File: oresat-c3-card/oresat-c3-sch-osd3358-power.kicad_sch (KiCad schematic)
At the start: 36 parts, among them Q6 MMBT2907, U1 OSD3358-1G-ISM, U10 SN74AUC1G07DCKR, U14 TLVH431

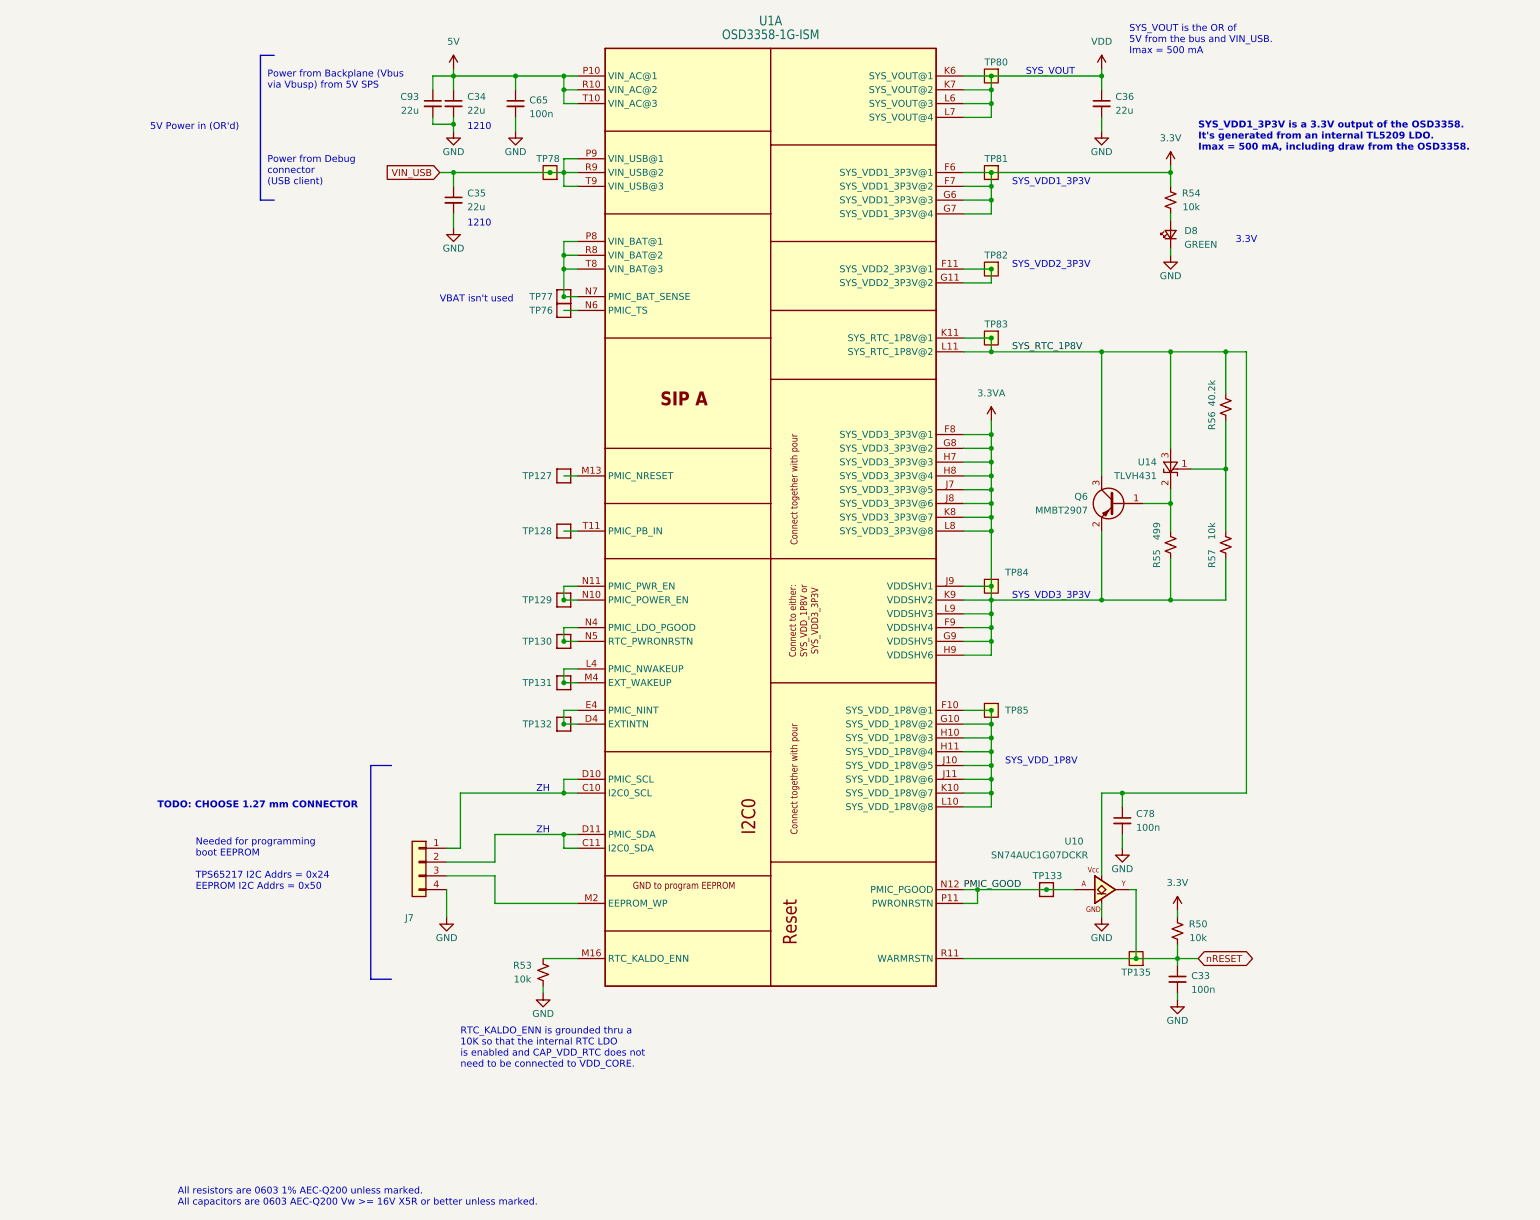
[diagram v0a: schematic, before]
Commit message: All DRC exclusing RF traces are cleaned up.  RF traces cleaned up with mask and bends. Some more notes in the schematic for future us.
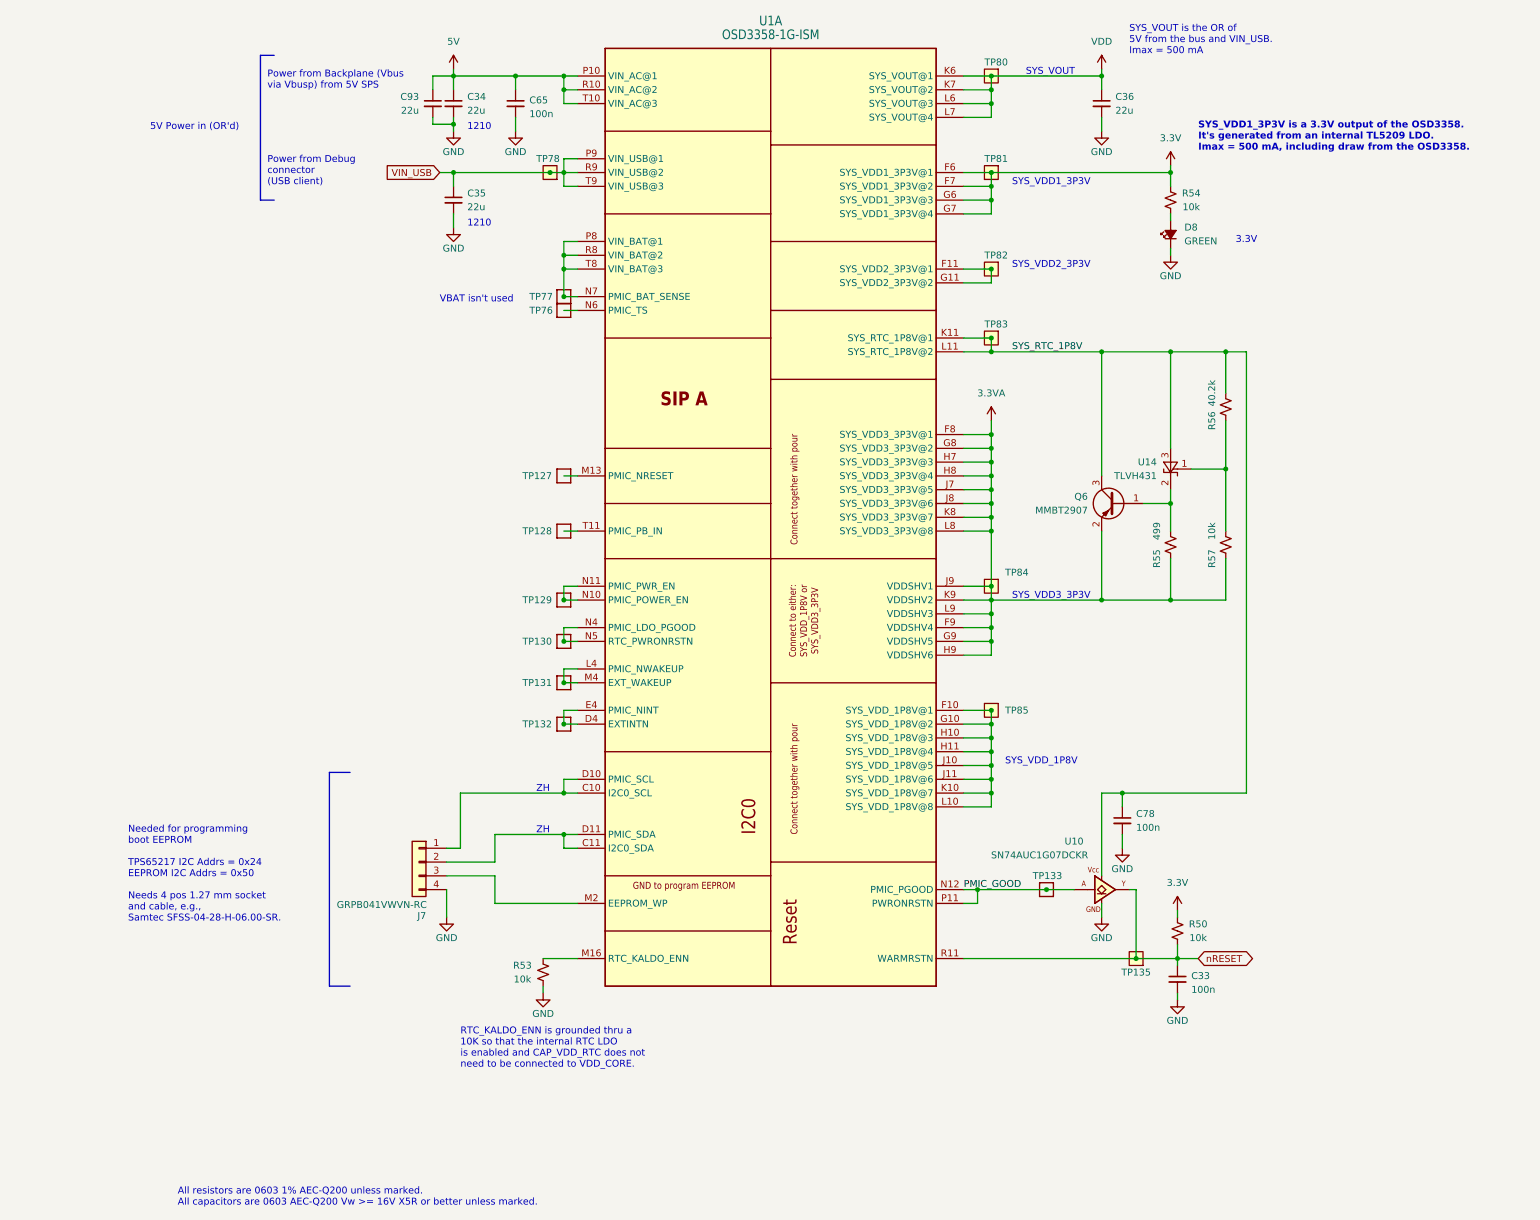
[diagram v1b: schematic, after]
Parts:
- D8: symbol Device:LED_Small -> Device:LED_Small_Filled
- J7: value ~ -> GRPB041VWVN-RC; DPN (none) -> S9014E-04-ND; DST (none) -> DigiKey; MFR (none) -> Sullins Connector Solutions; MPN (none) -> GRPB041VWVN-RC
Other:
- note added: "Needed for programming boot EEPROM TPS65217 I2C Addrs = 0x24 EEPROM I2C Addrs = 0x50 Needs 4 pos 1.27 mm socket and cable, e.g., Samtec SFSS-04-28-H-06.00-SR."
- note removed: "Needed for programming boot EEPROM TPS65217 I2C Addrs = 0x24 EEPROM I2C Addrs = 0x50"
- note removed: "TODO: CHOOSE 1.27 mm CONNECTOR"
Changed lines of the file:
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@@
 		)
 	)
-	(text "TODO: CHOOSE 1.27 mm CONNECTOR"
-		(exclude_from_sim no)
-		(at 130.302 187.706 0)
-		(effects
-			(font
-				(size 1.27 1.27)
-				(thickness 0.254)
-				(bold yes)
-			)
-		)
-	)
 	(text "All resistors are 0603 1% AEC-Q200 unless marked.\nAll capacitors are 0603 AEC-Q200 Vw >= 16V X5R or better unless marked."
 		(exclude_from_sim no)
@@
 		)
 	)
-	(text "Needed for programming\nboot EEPROM\n\nTPS65217 I2C Addrs = 0x24\nEEPROM I2C Addrs = 0x50"
+	(text "Needed for programming\nboot EEPROM\n\nTPS65217 I2C Addrs = 0x24\nEEPROM I2C Addrs = 0x50\n\nNeeds 4 pos 1.27 mm socket\nand cable, e.g., \nSamtec SFSS-04-28-H-06.00-SR."
 		(exclude_from_sim no)
-		(at 118.872 203.454 0)
+		(at 106.426 209.296 0)
 		(effects
 			(font
@@
 	(polyline
 		(pts
-			(xy 151.13 219.71) (xy 154.94 219.71)
+			(xy 143.51 220.98) (xy 147.32 220.98)
 		)
 		(stroke
@@
 	(polyline
 		(pts
-			(xy 154.94 180.34) (xy 151.13 180.34)
+			(xy 147.32 181.61) (xy 143.51 181.61)
 		)
 		(stroke
@@
 	(polyline
 		(pts
-			(xy 151.13 180.34) (xy 151.13 219.71)
+			(xy 143.51 181.61) (xy 143.51 220.98)
 		)
 		(stroke
@@
 	)
 	(symbol
-		(lib_id "Device:LED_Small")
+		(lib_id "Device:LED_Small_Filled")
 		(at 298.45 82.55 90)
 		(unit 1)
@@
 		(fields_autoplaced yes)
 		(property "Reference" "D8"
-			(at 300.99 81.8515 90)
+			(at 300.99 81.2164 90)
 			(effects
 				(font
@@
 		)
 		(property "Value" "GREEN"
-			(at 300.99 84.3915 90)
+			(at 300.99 83.7564 90)
 			(effects
 				(font
@@
 			)
 		)
-		(property "Datasheet" "https://www.we-online.com/components/products/datasheet/150060GS75000.pdf"
+		(property "Datasheet" "~"
 			(at 298.45 82.55 90)
 			(effects
@@
 			)
 		)
-		(property "Description" "Green 520nm LED Indication - Discrete 3.2V 0603 (1608 Metric) - 430 mcd @ 20 mA"
+		(property "Description" "Light emitting diode, small symbol, filled shape"
 			(at 298.45 82.55 0)
 			(effects
@@
 		(dnp no)
 		(property "Reference" "J7"
-			(at 158.242 208.4183 0)
+			(at 160.528 208.026 0)
 			(effects
 				(font
@@
 			)
 		)
-		(property "Value" "~"
-			(at 158.242 205.994 0)
+		(property "Value" "GRPB041VWVN-RC"
+			(at 153.162 205.994 0)
 			(effects
 				(font
@@
 			)
 		)
-		(property "Datasheet" "~"
+		(property "Datasheet" "https://s3.amazonaws.com/catalogspreads-pdf/PAGE94-95%20.050%20MALE%20HDR%20ST%20RA%20SMT.pdf"
+			(at 160.02 198.12 0)
+			(effects
+				(font
+					(size 1.27 1.27)
+				)
+				(hide yes)
+			)
+		)
+		(property "Description" "Connector Header Through Hole 4 position 0.050\" (1.27mm)"
+			(at 160.02 198.12 0)
+			(effects
+				(font
+					(size 1.27 1.27)
+				)
+				(hide yes)
+			)
+		)
+		(property "DPN" "S9014E-04-ND"
+			(at 160.02 198.12 0)
+			(effects
+				(font
+					(size 1.27 1.27)
+				)
+				(hide yes)
+			)
+		)
+		(property "DST" "DigiKey"
+			(at 160.02 198.12 0)
+			(effects
+				(font
+					(size 1.27 1.27)
+				)
+				(hide yes)
+			)
+		)
+		(property "MFR" "Sullins Connector Solutions"
 			(at 160.02 198.12 0)
 			(effects
@@
 			)
 		)
-		(property "Description" "Generic connector, single row, 01x04, script generated (kicad-library-utils/schlib/autogen/connector/)"
+		(property "MPN" "GRPB041VWVN-RC"
 			(at 160.02 198.12 0)
 			(effects

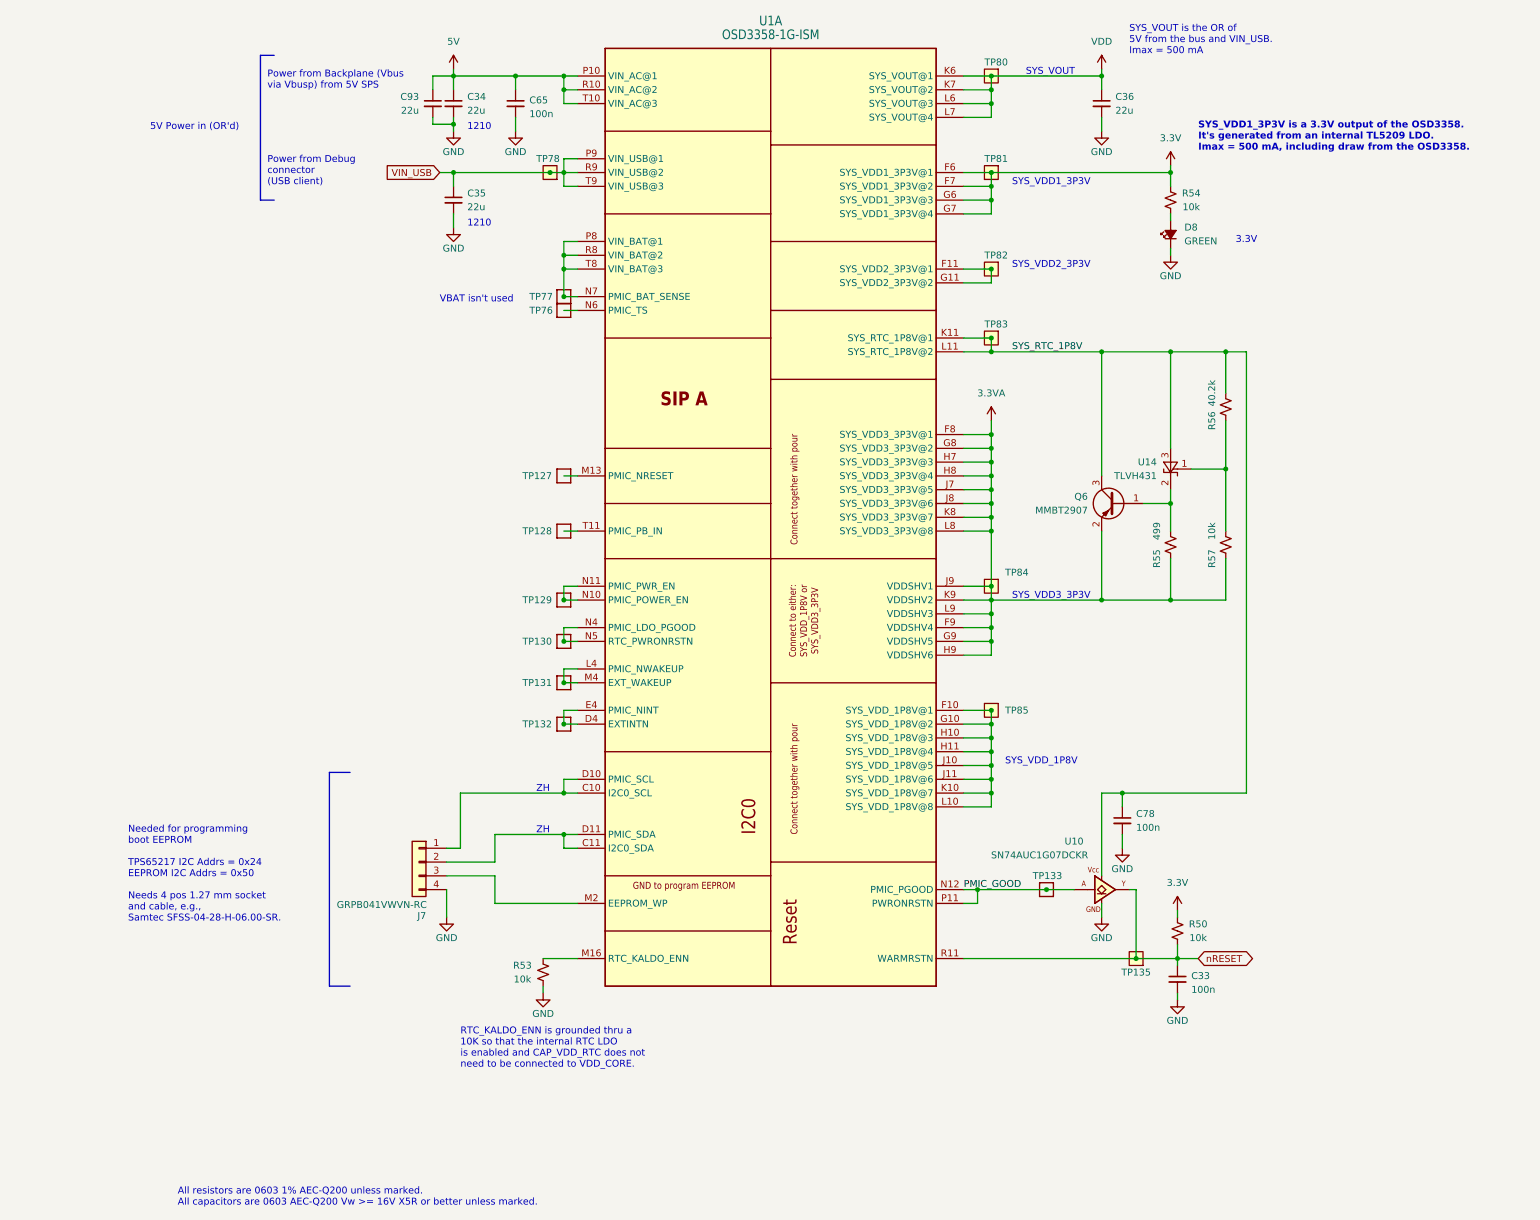
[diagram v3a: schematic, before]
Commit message: Minor polishing on schematic, mostly text notes.
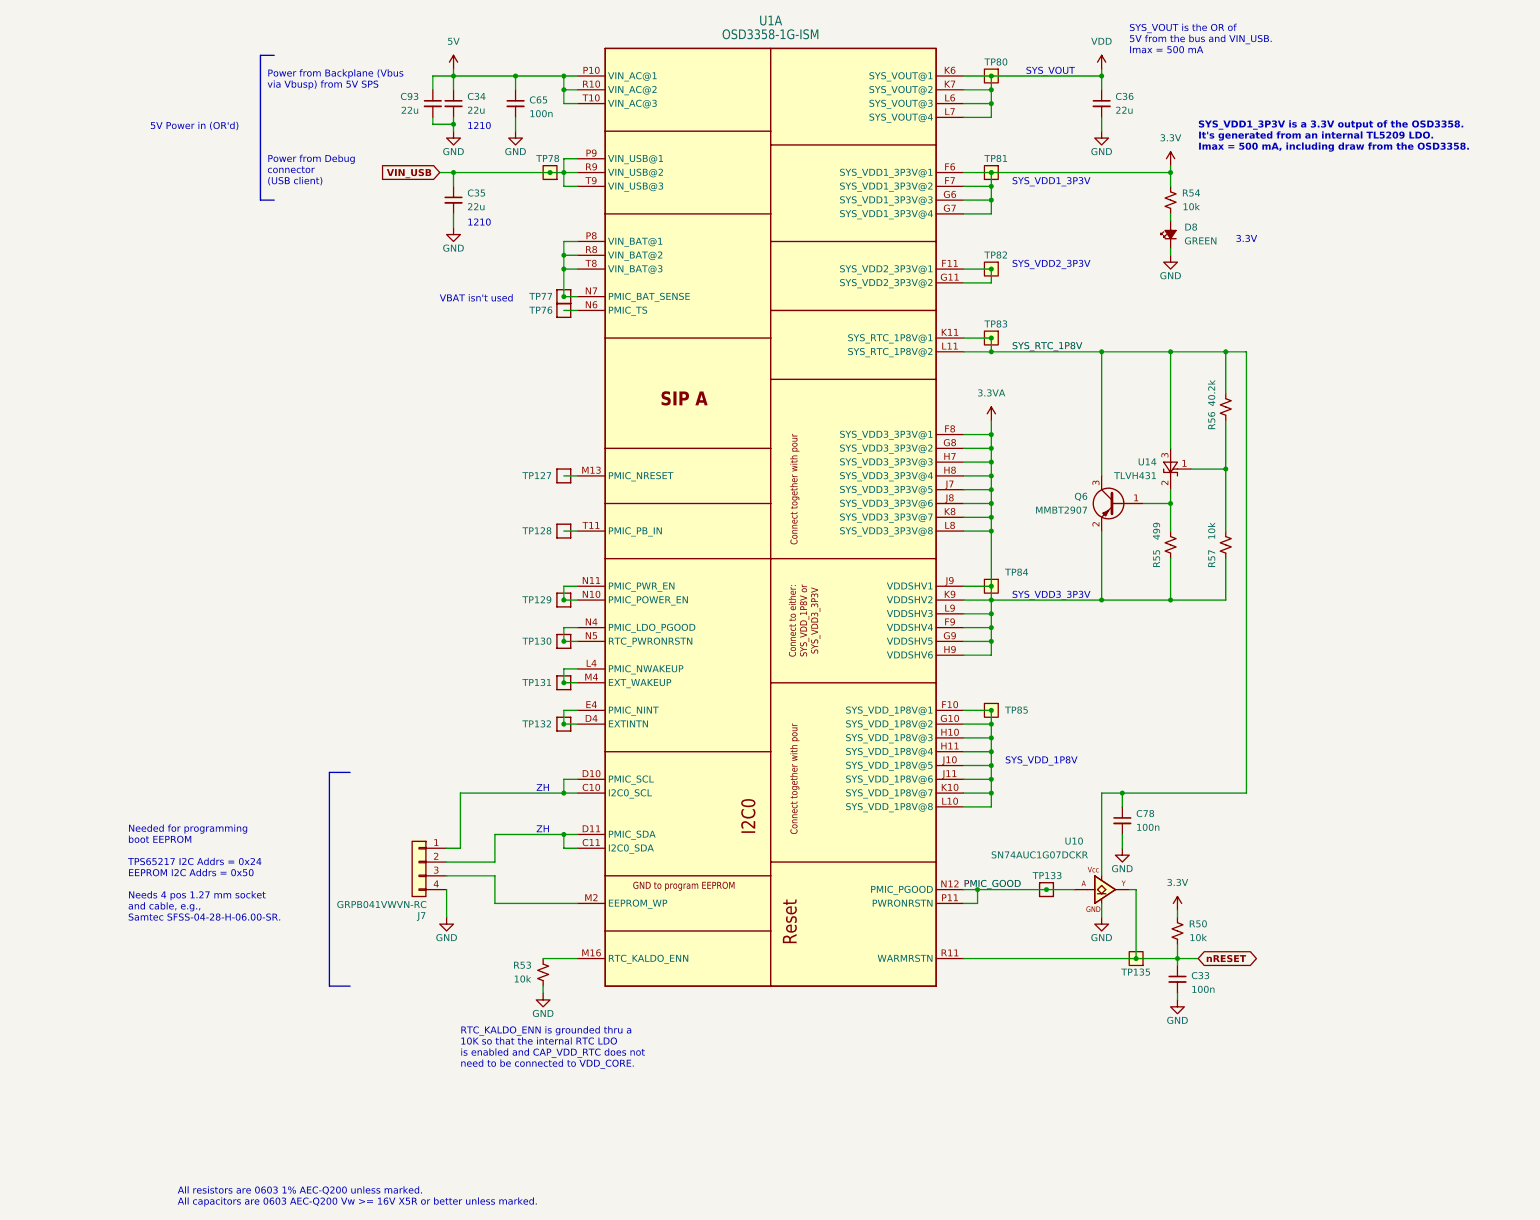
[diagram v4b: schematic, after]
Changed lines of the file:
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@@
 			(font
 				(size 1.27 1.27)
+				(thickness 0.254)
+				(bold yes)
 			)
 			(justify right)
@@
 			(font
 				(size 1.27 1.27)
+				(thickness 0.254)
+				(bold yes)
 			)
 			(justify left)
